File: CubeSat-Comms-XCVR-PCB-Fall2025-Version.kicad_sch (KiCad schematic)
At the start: 70 parts, among them J1 Conn_01x02_Pin, J2 Conn_01x02_Pin, J3 Conn_Coaxial, J4 Conn_01x12_Pin, U1 CC1101RGP, U2 SKY65366-21, U3 PE4251MLI-Z, U4 NCP186AMX390TAG, Y1 NX3225GA-26MHZ-TI

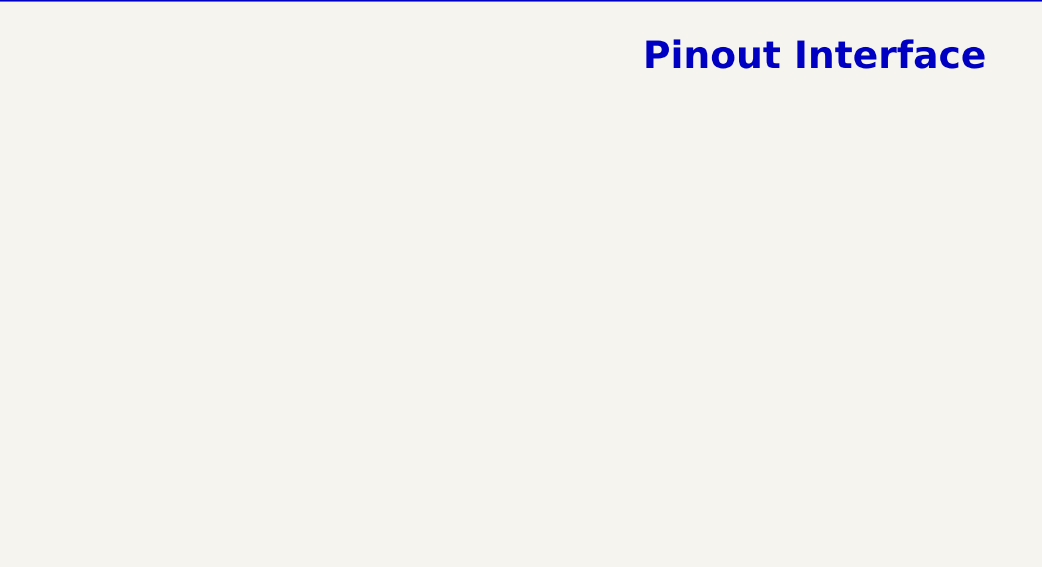
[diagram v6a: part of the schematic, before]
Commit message: test points and silkscreen
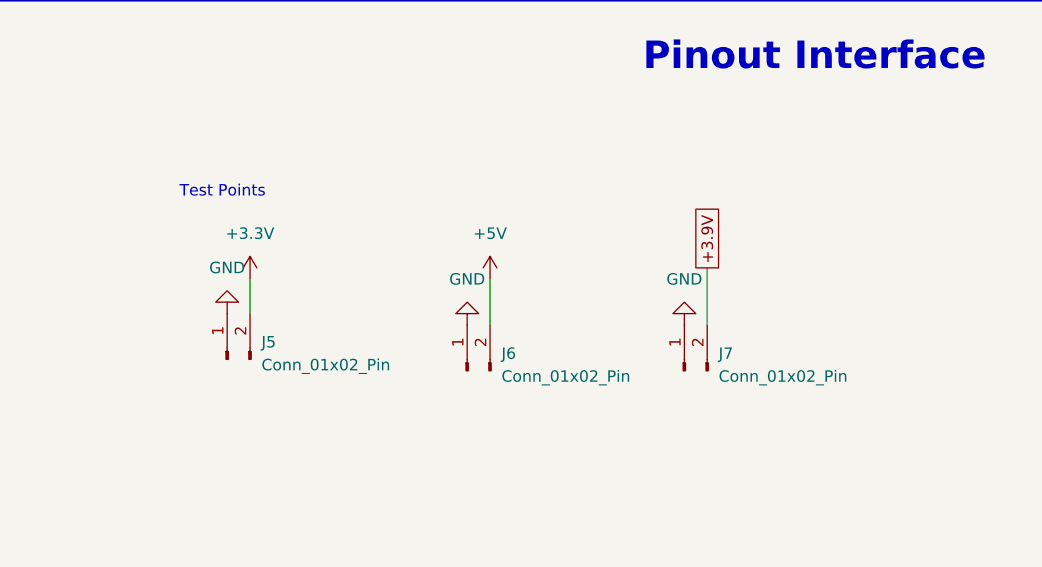
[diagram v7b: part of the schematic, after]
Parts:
- added J5, J6, J7: Conn_01x02_Pin, Connector_PinHeader_2.54mm:PinHeader_1x02_P2.54mm_Vertical, symbol Connector:Conn_01x02_Pin
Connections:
- net +3.3V: now also J5.2 (Pin_2)
- net +3.9V: now also J7.2 (Pin_2)
- net +5V: now also J6.2 (Pin_2)
- net GND: now also J5.1 (Pin_1), J6.1 (Pin_1), J7.1 (Pin_1)
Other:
- note added: "Test Points"

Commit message: added external signal injecting capability
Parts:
- added C27, C32: 220pF, comms-board-footprints-passives:G-188_MUR-L-100nF-GRM188, symbol Device:C
- added C33: 68pF, comms-board-footprints-passives:G-188_MUR-L-100nF-GRM188, symbol Device:C
- added J10: Conn_Coaxial, Connector_Coaxial:SMA_Amphenol_132134-11_Vertical, symbol Connector:Conn_Coaxial
- added J12: Conn_01x04_Pin, Connector_PinHeader_2.54mm:PinHeader_1x04_P2.54mm_Vertical, symbol Connector:Conn_01x04_Pin
- added J8, J9: Conn_01x02_Pin, Connector_PinSocket_2.54mm:PinSocket_1x02_P2.54mm_Vertical, symbol Connector:Conn_01x02_Pin
- added U5: PE4251MLI-Z, comms-board-footprints:8-MSOP_PE4251_PSM, symbol comms-board-symbols:PE4251MLI-Z
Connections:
- net +3.3V: now also J12.1 (Pin_1), J8.2 (Pin_2)
- net +5V: now also C32.2, J9.2 (Pin_2)
- net GND: now also J3.2 (Ext), C27.1, J10.2 (Ext), J12.4 (Pin_4), J8.1 (Pin_1), J9.1 (Pin_1), U5.4 (NC), U5.6 (GND), U5.7 (GND), U5.9 (GND); no longer J3.1 (In)
- net TX: now also U5.3 (RFC); no longer C18.1
- net at C29.1, C31.1, L5.1: now also J3.1 (In); no longer J3.2 (Ext)
- new net: C33.1, J10.1 (In)
- new net: C32.1, U5.1 (V2)
- new net: C33.2, U5.8 (RF2)
- new net TX_JUMP: C18.1, U5.5 (RF1)
- new net TX_SEL: C27.2, J12.2 (Pin_2), J12.3 (Pin_3), U5.2 (V1)
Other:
- note added: "Alternative MCU powwer"
- note added: "RF Switch 1"
- note added: "RF Switch 2"
- note added: "Single-pin control mode"
- note added: "V1 | V2 | Signal ------------ HIGH | 5V | RF1 ------------ LOW | 5V | RF2"
- note added: "V1 | V2 | Signal --------------- HIGH | LOW | RF1 --------------- LOW | HIGH | RF2"
- note added: "When I pull pin 2 LOW via jumper, inject external signals via external RF signal generator Ideally this should be trigged on HIGH, but orientation issues present"
- note removed: "RF Switch"
- note removed: "V1 | V2 | Selected ----------------- HIGH | LOW | RF1 ----------------- LOW | HIGH | RF2"
- moved on the sheet: C19, C21, D1, D3, D4, D5, D7, H1, H2, H3, H4, J1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
